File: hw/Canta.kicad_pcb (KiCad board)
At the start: 2 copper layers, 85.6 x 54 mm, 0 parts

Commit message: Layout, I think
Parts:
- added C1: 10u, Capacitor_SMD:C_0603_1608Metric, F.Cu at (30.1, 21.1)
- added C10: 4.7u, Capacitor_SMD:C_0402_1005Metric, F.Cu at (50.5, 29.3)
- added C11: 4.7u, Capacitor_SMD:C_0402_1005Metric, F.Cu at (51.9, 20.6)
- added C2: 10n, Capacitor_SMD:C_0402_1005Metric, F.Cu at (31.3, 25.9)
- added C3: 100n, Capacitor_SMD:C_0402_1005Metric, F.Cu at (37.1, 26.9)
- added C4: 6.8p, Capacitor_SMD:C_0402_1005Metric, F.Cu at (31.5, 27.1)
- added C5: 6.8p, Capacitor_SMD:C_0402_1005Metric, F.Cu at (32.5, 32.3)
- added C6: 10u, Capacitor_SMD:C_0603_1608Metric, F.Cu at (42.6, 28.5)
- added C7: 100n, Capacitor_SMD:C_0402_1005Metric, F.Cu at (42.6, 27.2)
- added C8: 4.7n, Capacitor_SMD:C_0402_1005Metric, F.Cu at (47.3, 24.2)
- added C9: 470n, Capacitor_SMD:C_0402_1005Metric, F.Cu at (47.3, 22.3)
- added D1: Pink, LED_SMD:LED_0603_1608Metric, F.Cu at (33.1, 23.5)
- added J1: USB_C_Receptacle_PowerOnly_6P, Canta_footprints:USB_C_Receptacle, F.Cu at (24.1, 25.8)
- added J101: Conn_01x01, Canta_footprints:TouchPad_Keyboard, F.Cu at (24.5, 63.2)
- added J102: Conn_01x01, Canta_footprints:TouchPad_Keyboard, F.Cu at (33.0, 63.2)
- added J103: Conn_01x01, Canta_footprints:TouchPad_Keyboard, F.Cu at (41.5, 63.2)
- added J104: Conn_01x01, Canta_footprints:TouchPad_Keyboard, F.Cu at (50.0, 63.2)
- added J105: Conn_01x01, Canta_footprints:TouchPad_Keyboard, F.Cu at (58.5, 63.2)
- added J106: Conn_01x01, Canta_footprints:TouchPad_Keyboard, F.Cu at (67.0, 63.2)
- added J107: Conn_01x01, Canta_footprints:TouchPad_Keyboard, F.Cu at (75.5, 63.2)
- added J108: Conn_01x01, Canta_footprints:TouchPad_Keyboard, F.Cu at (84.0, 63.2)
- added J109: Conn_01x01, Canta_footprints:TouchPad_Keyboard, F.Cu at (92.5, 63.2)
- added J110: Conn_01x01, Canta_footprints:TouchPad_Keyboard, F.Cu at (101.0, 63.2)
- added J111: Conn_01x01, Canta_footprints:TouchPad_Transpose, F.Cu at (27.4, 45.0)
- added J112: Conn_01x01, Canta_footprints:TouchPad_Transpose, F.Cu at (98.0, 44.6)
- added J2: Conn_01x03, Canta_footprints:TestPoints_1x03_P2.0, F.Cu at (35.0, 21.0)
- added JP1: SolderJumper_2_Open, Canta_footprints:SolderJumper-2_Open, F.Cu at (36.3, 25.1)
- added JP2: SolderJumper_2_Open, Canta_footprints:SolderJumper-2_Open, F.Cu at (34.9, 25.1)
- added LS1: Speaker, Canta_footprints:Speaker_1x02_P2, F.Cu at (50.6, 31.3)
- added R1: 5.1k, Resistor_SMD:R_0402_1005Metric, F.Cu at (29.6, 26.5)
- added R101: 470k, Resistor_SMD:R_0402_1005Metric, F.Cu at (32.6, 34.3)
- added R102: 470k, Resistor_SMD:R_0402_1005Metric, F.Cu at (33.7, 34.3)
- added R103: 470k, Resistor_SMD:R_0402_1005Metric, F.Cu at (34.8, 34.3)
- added R104: 470k, Resistor_SMD:R_0402_1005Metric, F.Cu at (35.9, 34.3)
- added R105: 470k, Resistor_SMD:R_0402_1005Metric, F.Cu at (37.0, 34.3)
- added R106: 470k, Resistor_SMD:R_0402_1005Metric, F.Cu at (38.1, 34.3)
- added R107: 470k, Resistor_SMD:R_0402_1005Metric, F.Cu at (39.2, 34.3)
- added R108: 470k, Resistor_SMD:R_0402_1005Metric, F.Cu at (40.3, 34.3)
- added R109: 470k, Resistor_SMD:R_0402_1005Metric, F.Cu at (41.4, 34.3)
- added R110: 470k, Resistor_SMD:R_0402_1005Metric, F.Cu at (42.5, 34.3)
- added R111: 470k, Resistor_SMD:R_0402_1005Metric, F.Cu at (31.5, 34.3)
- added R112: 470k, Resistor_SMD:R_0402_1005Metric, F.Cu at (43.6, 34.3)
- added R2: 5.1k, Resistor_SMD:R_0402_1005Metric, F.Cu at (28.6, 26.5)
- added R3: 7.5k, Resistor_SMD:R_0402_1005Metric, F.Cu at (33.5, 26.0)
- added R4: 470, Resistor_SMD:R_0402_1005Metric, F.Cu at (46.3, 24.2)
- added R5: 22k, Resistor_SMD:R_0402_1005Metric, F.Cu at (49.2, 20.6)
- added R6: 50k, Potentiometer_SMD:Potentiometer_Bourns_TC33X_Vertical, F.Cu at (46.2, 31.3)
- added U1: SPX3819M5-L-3-3, Package_TO_SOT_SMD:SOT-23-5, F.Cu at (30.2, 23.7)
- added U2: PY32F003F18U6, Package_DFN_QFN:QFN-20-1EP_3x3mm_P0.4mm_EP1.65x1.65mm, F.Cu at (35.8, 29.6)
- added U3: TM8211, TM8211:SOIC127P600X196-8N, F.Cu at (42.0, 23.9)
- added U4: FM8002A, Package_SO:SOP-8_3.9x4.9mm_P1.27mm, F.Cu at (50.6, 24.9)
- added Y1: 32MHz 12pF, Crystal:Crystal_SMD_3225-4Pin_3.2x2.5mm, F.Cu at (31.9, 29.7)
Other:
- board text added: "Canta-Cart"

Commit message: Routing, I think
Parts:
- moved R5 1.04 mm to (48.1, 20.6), turned to 0 degrees
- moved J112 0.90 mm to (98.8, 45.0)
- moved J111 0.63 mm to (26.8, 45.0)
- moved C3 0.58 mm to (37.3, 27.4)
- moved Y1 0.50 mm to (32.1, 30.2)
- moved U2 0.50 mm to (36.0, 30.0)
- moved C4 0.50 mm to (31.6, 27.6)
- moved R101 0.50 mm to (32.7, 34.8)
- moved R102 0.50 mm to (33.8, 34.8)
- moved R103 0.50 mm to (34.9, 34.8)
- moved R104 0.50 mm to (36.0, 34.8)
- moved R105 0.50 mm to (37.1, 34.8)
- moved R106 0.50 mm to (38.2, 34.8)
- moved R107 0.50 mm to (39.3, 34.8)
- moved R108 0.50 mm to (40.4, 34.8)
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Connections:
- JP1 pad 2: BTN_09 -> BTN_10
- JP2 pad 2: BTN_10 -> BTN_12
- U2 pad 1: BTN_05 -> BTN_06
- U2 pad 15: BTN_12 -> BTN_01
- U2 pad 16: BTN_01 -> BTN_02
- U2 pad 18: BTN_02 -> BTN_03
- U2 pad 19: BTN_03 -> BTN_04
- U2 pad 2: BTN_06 -> BTN_07
- U2 pad 20: BTN_04 -> BTN_05
- U2 pad 3: BTN_07 -> BTN_08
- U2 pad 5: BTN_08 -> BTN_09
- U2 pad 7: BTN_09 -> BTN_10
- U2 pad 8: BTN_10 -> BTN_12
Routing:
- net BTN_10: track 0.00 -> 89.0 mm
- net BTN_12: track 0.00 -> 79.0 mm
- net BTN_09: track 0.00 -> 74.2 mm
- net BTN_08: track 0.00 -> 65.6 mm
- net BTN_07: track 0.00 -> 57.3 mm
- net BTN_06: track 0.00 -> 49.0 mm
- net +3.3V: track 0.00 -> 42.5 mm, vias 0 -> 5
- net BTN_05: track 0.00 -> 40.7 mm
- net BTN_04: track 0.00 -> 37.6 mm
- net BTN_01: track 0.00 -> 37.1 mm
- net BTN_03: track 0.00 -> 34.9 mm
- net BTN_02: track 0.00 -> 33.0 mm
- net BTN_OUT: track 0.00 -> 27.9 mm, vias 0 -> 13
- net BTN_11: track 0.00 -> 26.4 mm
- net GND: track 0.00 -> 22.4 mm, vias 0 -> 46
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- added copper zone on B.Cu, net GND
- added copper zone on F.Cu, net GND

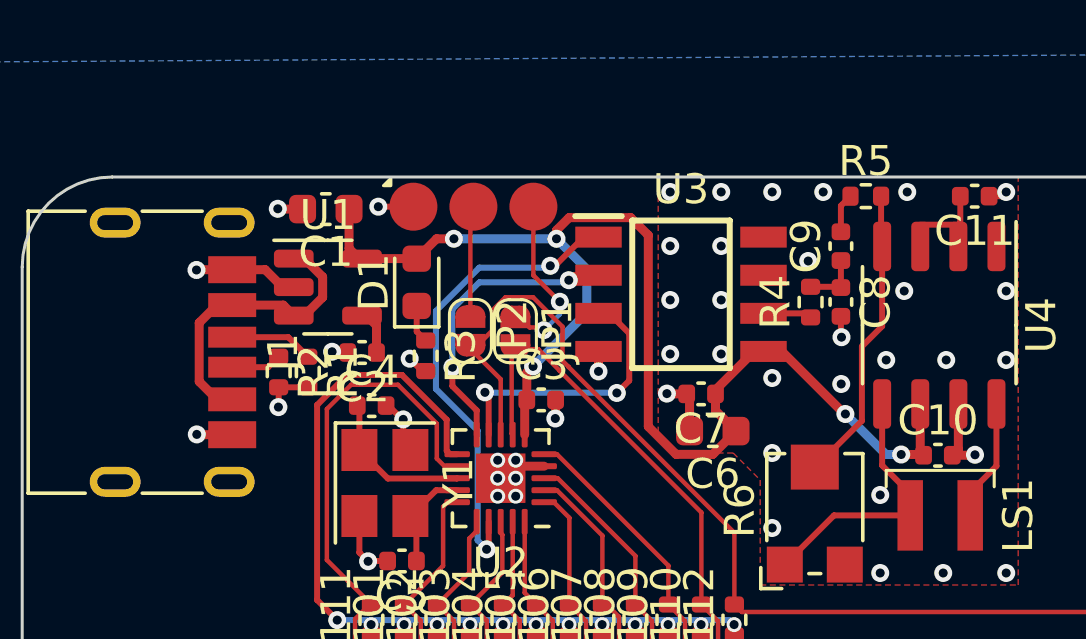
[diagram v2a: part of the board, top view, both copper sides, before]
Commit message: Switch supplies of audio ICs to 5 V
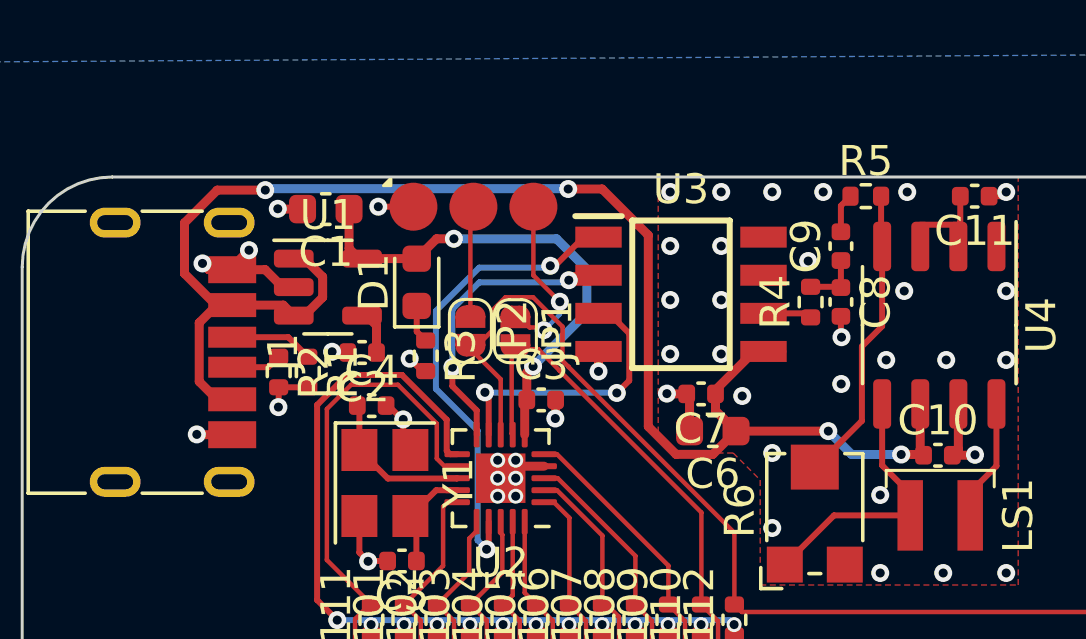
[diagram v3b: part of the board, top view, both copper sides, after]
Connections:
- C10 pad 1: +3.3V -> +5V
- C6 pad 1: +3.3V -> +5V
- C7 pad 1: +3.3V -> +5V
- U3 pad 5: +3.3V -> +5V
- U4 pad 6: +3.3V -> +5V
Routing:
- net +5V: track 9.96 -> 53.0 mm, vias 0 -> 4
- net +3.3V: track 42.5 -> 16.4 mm, vias 5 -> 2
- net GND: track 22.4 -> 23.2 mm, vias 46 -> 47

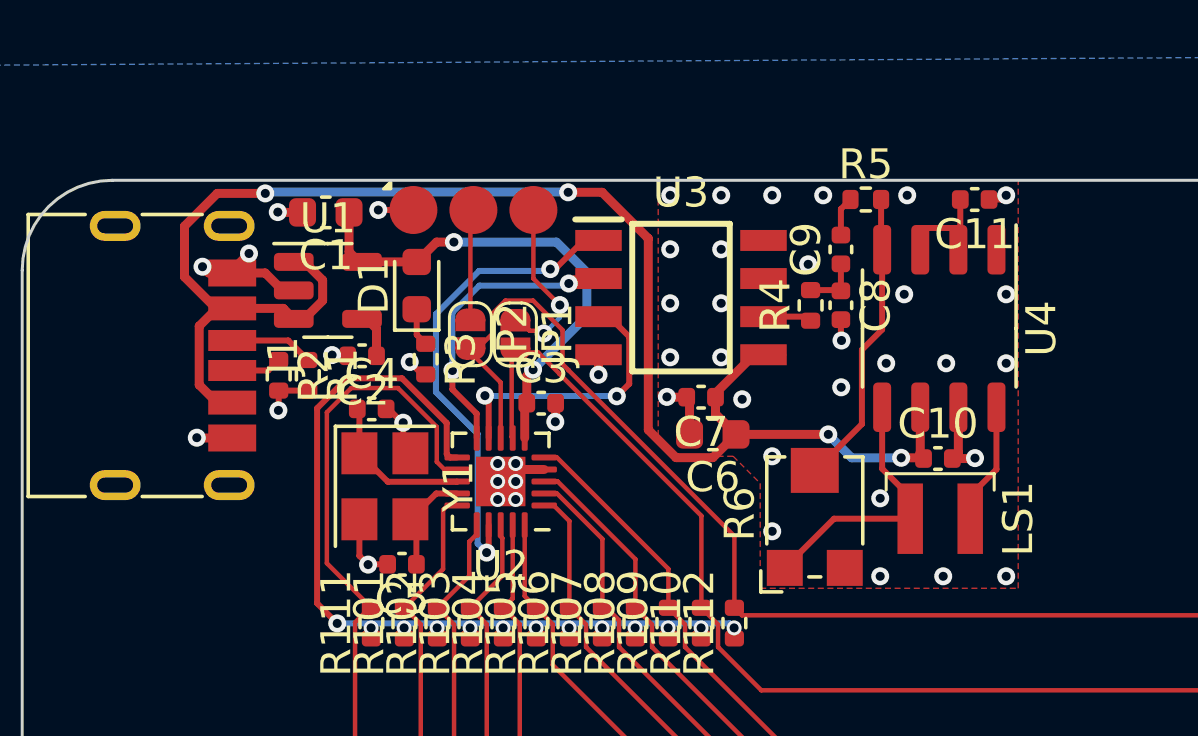
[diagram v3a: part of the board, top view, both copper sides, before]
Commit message: Modify entire circuit to run on 5 V
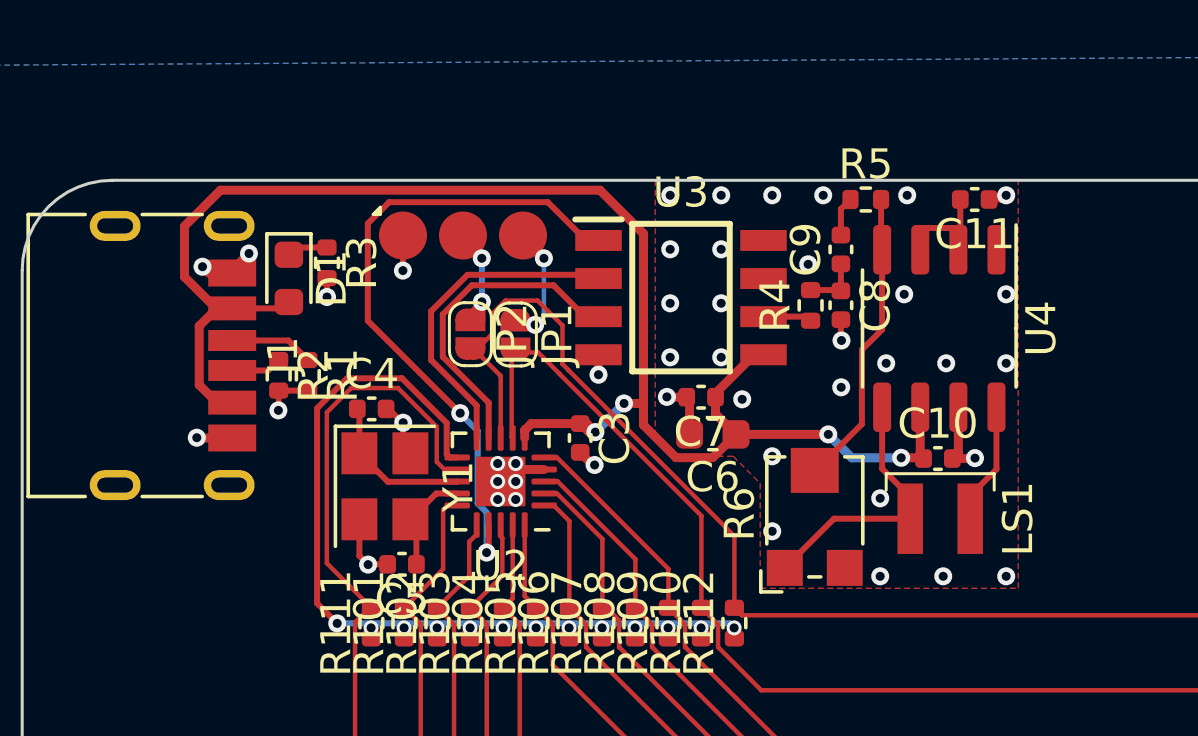
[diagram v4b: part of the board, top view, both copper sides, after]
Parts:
- removed C1: 10u, Capacitor_SMD:C_0603_1608Metric
- removed C2: 10n, Capacitor_SMD:C_0402_1005Metric
- removed U1: SPX3819M5-L-3-3, Package_TO_SOT_SMD:SOT-23-5
- moved R3 4.60 mm to (30.2, 22.8)
- moved D1 4.27 mm to (28.9, 23.3), turned to -90 degrees
- moved C3 1.74 mm to (38.6, 28.6), turned to -90 degrees
- moved J2 0.92 mm to (34.7, 21.8)
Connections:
- C3 pad 1: +3.3V -> +5V
- D1 pad 2: +3.3V -> +5V
- U2 pad 6: +3.3V -> +5V
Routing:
- net +3.3V: track 16.4 -> 0.00 mm, vias 2 -> 0
- net I2S_BCK: track 16.0 -> 22.1 mm
- net GND: track 23.2 -> 19.5 mm, vias 47 -> 45
- net +5V: track 53.0 -> 55.2 mm
- net SWDIO: track 5.89 -> 4.16 mm
- net Net-(U1-BP): track 1.52 -> 0.00 mm
- net I2S_DATA: track 9.33 -> 10.8 mm, vias 2 -> 0
- net I2S_WS: track 9.86 -> 11.0 mm, vias 2 -> 0
- net SWCLK: track 3.58 -> 3.82 mm, vias 0 -> 2

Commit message: Update silkscreen
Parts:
- R3: value 7.5k -> 10k
- renumbered C3 to C1, C4 to C2, C5 to C3, C6 to C4, C7 to C5, C8 to C6, C9 to C7, C10 to C8, C11 to C9, U2 to U1, U3 to U2, U4 to U3
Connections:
- C2 pad 1: Net-(U2-PF0) -> (no net)
- C3 pad 1: Net-(U2-PF1) -> (no net)
- C6 pad 1: Net-(C8-Pad1) -> (no net)
- C7 pad 1: Net-(C8-Pad1) -> Net-(C6-Pad1)
- C7 pad 2: Net-(C9-Pad2) -> (no net)
- C9 pad 2: Net-(U4-+IN) -> (no net)
- R4 pad 2: Net-(C8-Pad1) -> Net-(C6-Pad1)
- R5 pad 1: Net-(C9-Pad2) -> Net-(C7-Pad2)
- U1 pad 13: Net-(U2-PF0) -> Net-(U1-PF0)
- U1 pad 14: Net-(U2-PF1) -> Net-(U1-PF1)
- U2 pad 7: unconnected-(U3-NC-Pad7) -> (no net)
- U2 pad 8: unconnected-(U3-RCH-Pad8) -> (no net)
- U3 pad 1: unconnected-(U4-SD-Pad1) -> (no net)
- U3 pad 2: Net-(U4-+IN) -> Net-(U3-+IN)
- U3 pad 3: Net-(U4-+IN) -> Net-(U3-+IN)
- Y1 pad 1: Net-(U2-PF0) -> Net-(U1-PF0)
- Y1 pad 3: Net-(U2-PF1) -> Net-(U1-PF1)
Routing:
- net Net-(U2-PF0): track 5.17 -> 0.00 mm
- net Net-(U1-PF0): track 0.00 -> 5.17 mm
- net Net-(U2-PF1): track 3.50 -> 0.00 mm
- net Net-(U1-PF1): track 0.00 -> 3.50 mm
- net Net-(U4-+IN): track 2.97 -> 0.00 mm
- net Net-(U3-+IN): track 0.00 -> 2.97 mm
- net Net-(C8-Pad1): track 1.92 -> 0.00 mm
- net Net-(C6-Pad1): track 0.00 -> 1.92 mm
- net Net-(C9-Pad2): track 1.32 -> 0.00 mm
- net Net-(C7-Pad2): track 0.00 -> 1.32 mm

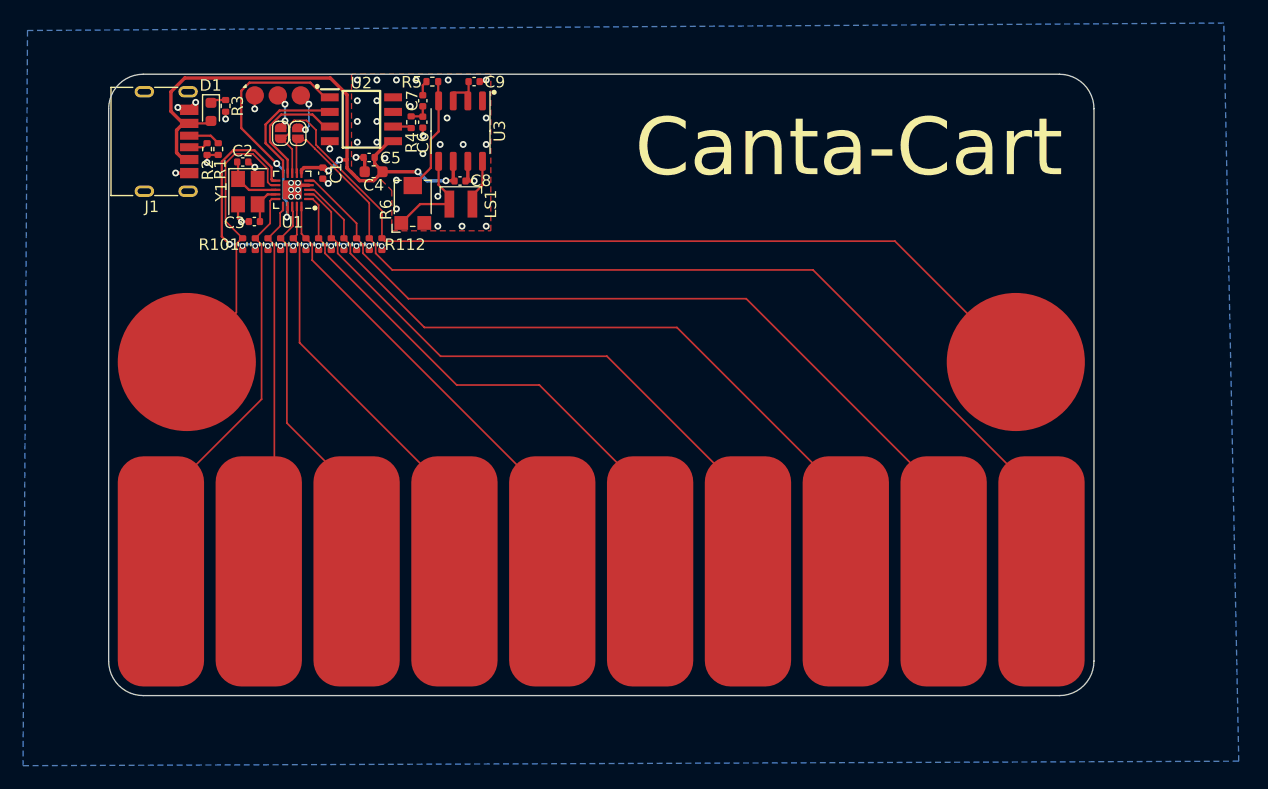
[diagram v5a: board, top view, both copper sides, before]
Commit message: Add back-side image
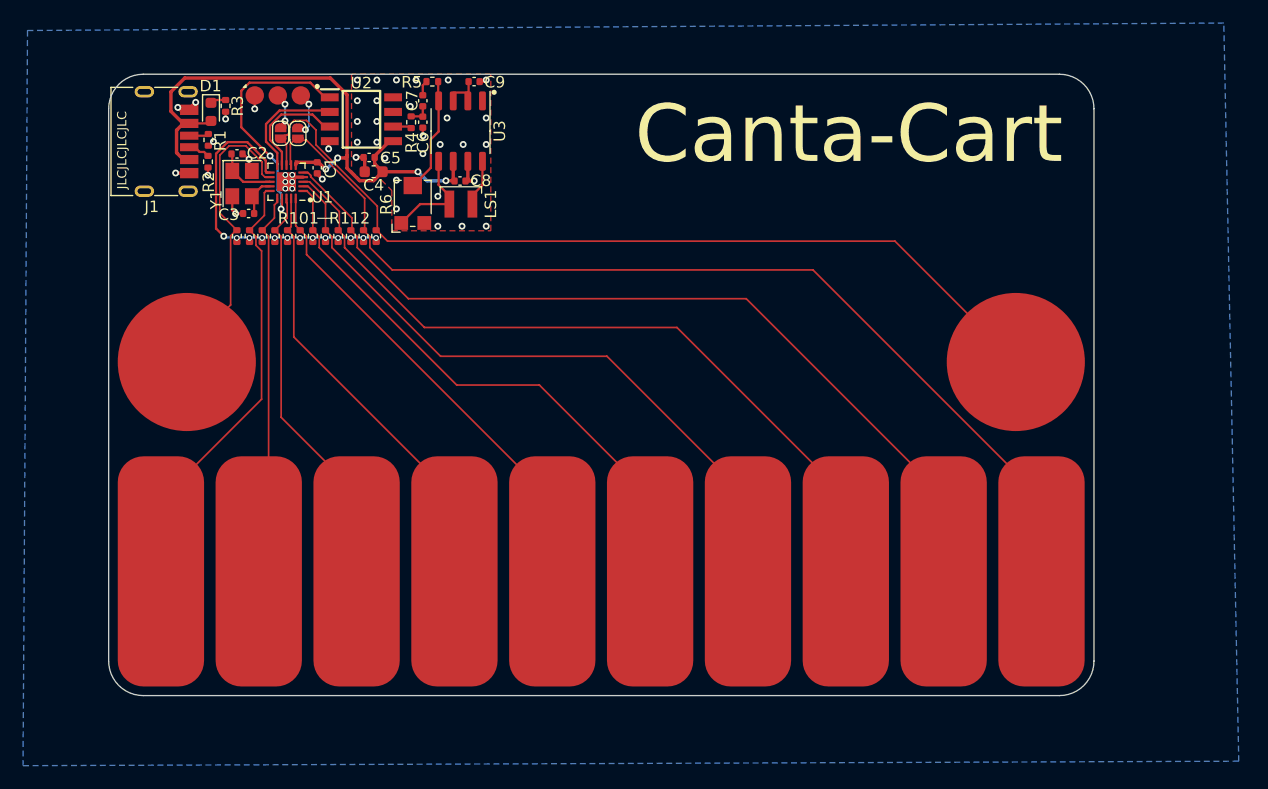
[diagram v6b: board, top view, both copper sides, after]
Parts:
- added G***: LOGO, LOGO, B.Cu at (102.1, 70.6)
- added G***: LOGO, LOGO, B.Cu at (97.1, 70.7)
- moved R1 1.17 mm to (28.7, 25.7)
- moved R2 1.10 mm to (28.6, 27.6)
- moved Y1 0.86 mm to (31.6, 29.5)
- moved C2 0.86 mm to (31.1, 26.9)
- moved U1 0.86 mm to (35.5, 29.3)
- moved C3 0.86 mm to (32.2, 32.1)
- moved R101 0.86 mm to (32.2, 34.1)
- moved R102 0.86 mm to (33.3, 34.1)
- moved R103 0.86 mm to (34.4, 34.1)
- moved R104 0.86 mm to (35.5, 34.1)
- moved R105 0.86 mm to (36.6, 34.1)
- moved R106 0.86 mm to (37.7, 34.1)
- moved R107 0.86 mm to (38.8, 34.1)
- moved R108 0.86 mm to (39.9, 34.1)
- moved R109 0.86 mm to (41.0, 34.1)
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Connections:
- C2 pad 1: (no net) -> Net-(U1-PF0)
- C3 pad 1: (no net) -> Net-(U1-PF1)
- C6 pad 1: (no net) -> Net-(C6-Pad1)
- C7 pad 2: (no net) -> Net-(C7-Pad2)
- C9 pad 2: (no net) -> Net-(U3-+IN)
- U2 pad 7: (no net) -> unconnected-(U2-NC-Pad7)
- U2 pad 8: (no net) -> unconnected-(U2-RCH-Pad8)
- U3 pad 1: (no net) -> unconnected-(U3-SD-Pad1)
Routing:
- net BTN_12: track 79.2 -> 77.6 mm
- net Net-(J1-CC1): track 2.79 -> 1.72 mm
- net BTN_08: track 65.6 -> 66.6 mm
- net BTN_09: track 74.2 -> 75.2 mm
- net I2S_WS: track 11.0 -> 10.0 mm
- net BTN_05: track 40.7 -> 41.6 mm
- net BTN_03: track 34.9 -> 35.8 mm
- net BTN_06: track 49.0 -> 49.9 mm
- net I2S_DATA: track 10.8 -> 9.87 mm
- net BTN_04: track 37.6 -> 38.5 mm
- net BTN_01: track 37.1 -> 38.0 mm
- net BTN_07: track 57.3 -> 58.2 mm
- net I2S_BCK: track 22.1 -> 21.3 mm
- net GND: track 19.5 -> 19.2 mm, vias 45 -> 46
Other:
- board text added: "24-Awn"
- board text added: "JLCJLCJLCJLC"
- board text added: "Rev. 2"
- board text added: "ayu.land/canta-cart"
- board text added: "—"
